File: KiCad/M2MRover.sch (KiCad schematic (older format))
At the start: 12 parts, among them J1 microbit_edge_connector, U1 ESP8266-ESP-01

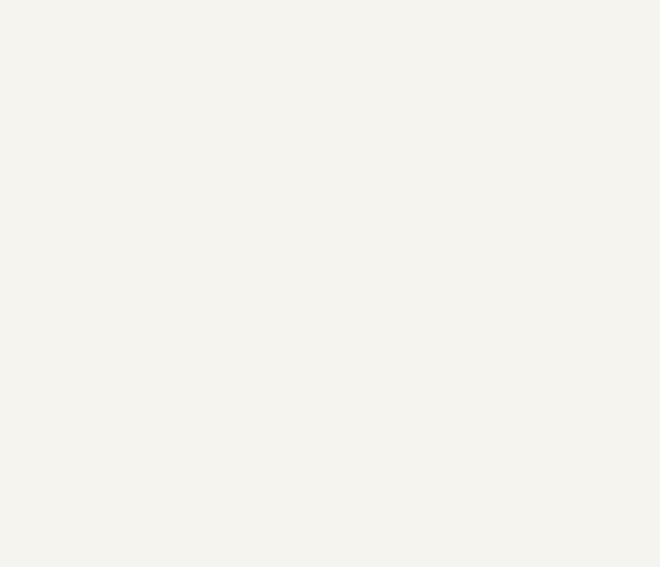
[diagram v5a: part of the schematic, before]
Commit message: Add Software Cornwall Log via symbol
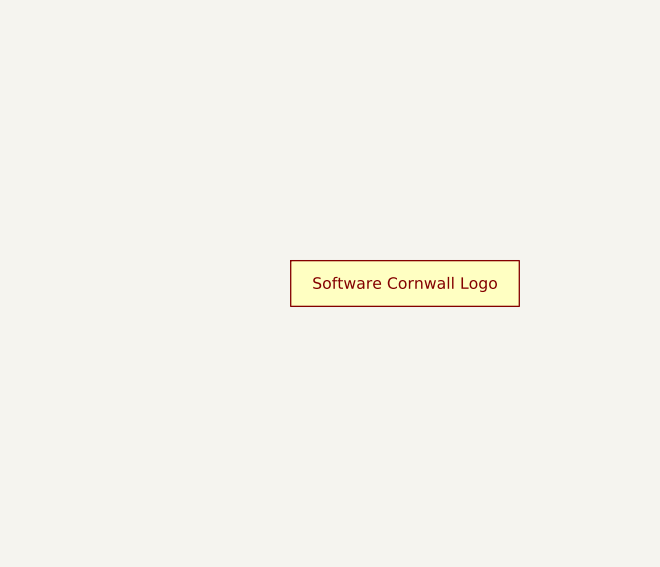
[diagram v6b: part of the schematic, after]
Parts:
- added LOGO1: Software_Cornwall_Logo, Software_Cornwall:SoftwareCornwallLogo, symbol SoftwareCornwall:Software_Cornwall_Logo
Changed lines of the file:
@@
 Wire Wire Line
 	2850 5800 3150 5800
+$Comp
+L SoftwareCornwall:Software_Cornwall_Logo LOGO1
+U 1 1 5D930A82
+P 10150 4950
+F 0 "LOGO1" H 10150 4800 50  0001 C CNN
+F 1 "Software_Cornwall_Logo" H 10150 5150 50  0001 C CNN
+F 2 "Software_Cornwall:SoftwareCornwallLogo" H 10150 4700 50  0001 C CNN
+F 3 "" H 10150 4950 50  0001 C CNN
+	1    10150 4950
+	1    0    0    -1
+$EndComp
 $EndSCHEMATC

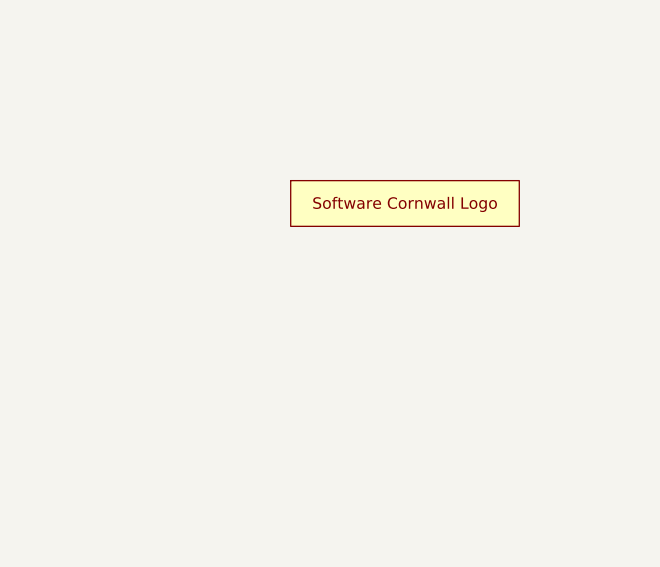
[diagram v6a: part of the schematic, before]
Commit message: Add JLCPCB order number to silk
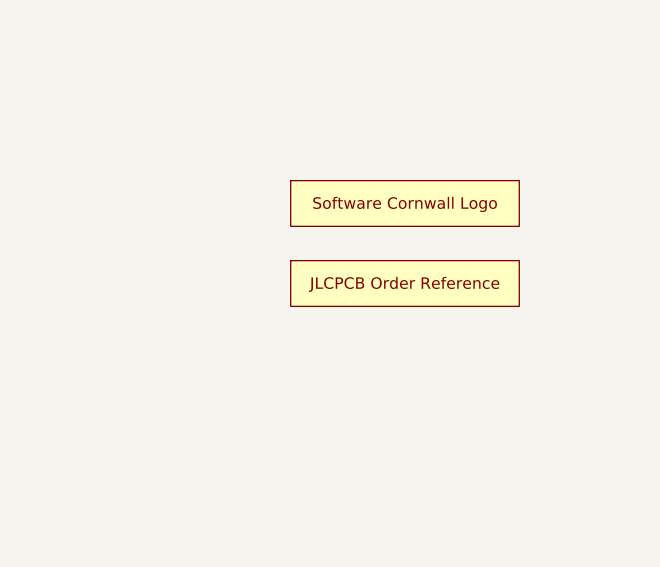
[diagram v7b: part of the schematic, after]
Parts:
- added ORDERNO1: JLCPCB_Order_Number, Software_Cornwall:JLCPCBOrderNumber, symbol SoftwareCornwall:JLCPCB_Order_Number
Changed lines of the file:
@@
+	1    0    0    -1
+$EndComp
+$Comp
+L SoftwareCornwall:JLCPCB_Order_Number ORDERNO1
+U 1 1 5D941D90
+P 10150 5300
+F 0 "ORDERNO1" H 10150 5150 50  0001 C CNN
+F 1 "JLCPCB_Order_Number" H 10150 5450 50  0001 C CNN
+F 2 "Software_Cornwall:JLCPCBOrderNumber" H 10150 5050 50  0001 C CNN
+F 3 "" H 10150 5300 50  0001 C CNN
+	1    10150 5300
 	1    0    0    -1
 $EndComp

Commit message: Change microbit connector footprint to use new custom footprint
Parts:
- J1: footprint MCU_Module_Microbit:4UCON_17909_02x401.27mm_Vertical -> Software_Cornwall:4UCON_10156_B3_Horizontal
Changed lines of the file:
@@
 F 0 "J1" H 1250 4875 50  0000 C CNN
 F 1 "microbit_edge_connector" H 1250 4784 50  0000 C CNN
-F 2 "MCU_Module_Microbit:4UCON_17909_02x401.27mm_Vertical" H 1150 2750 50  0001 C CNN
+F 2 "Software_Cornwall:4UCON_10156_B3_Horizontal" H 1150 2750 50  0001 C CNN
 F 3 "https://www.microbit.co.uk/device/pins" H 1150 2750 50  0001 C CNN
 	1    1250 2850
